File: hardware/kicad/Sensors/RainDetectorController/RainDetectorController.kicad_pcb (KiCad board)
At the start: 2 copper layers, 54.1 x 44.1 mm, 15 parts, among them J1 Conn_01x04_Socket, J2 Conn_01x04_Socket, J3 HEATER_CTRL, J4 RAIN_SIGNAL, Q1 AO3400A, U1 ICM7555xB

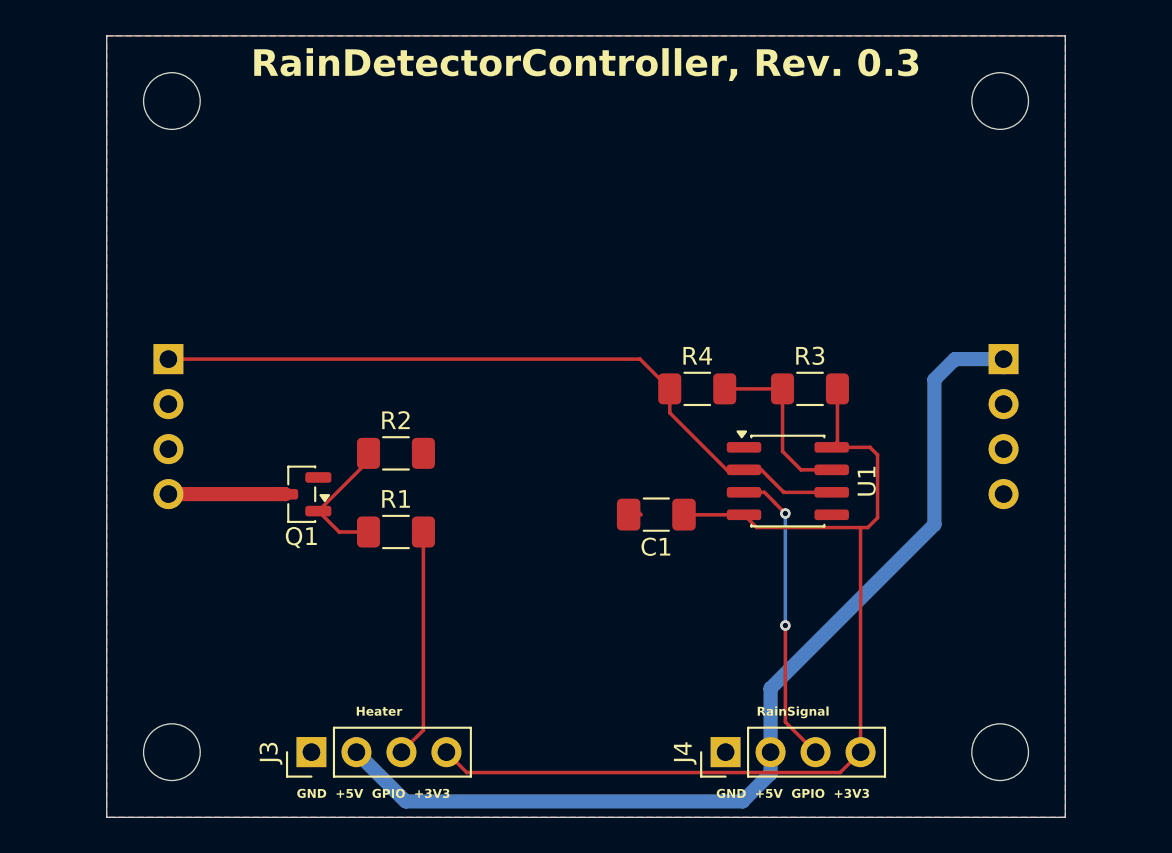
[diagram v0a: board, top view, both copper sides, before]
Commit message: modified Board-Geometry for RainDetector Head & Controller
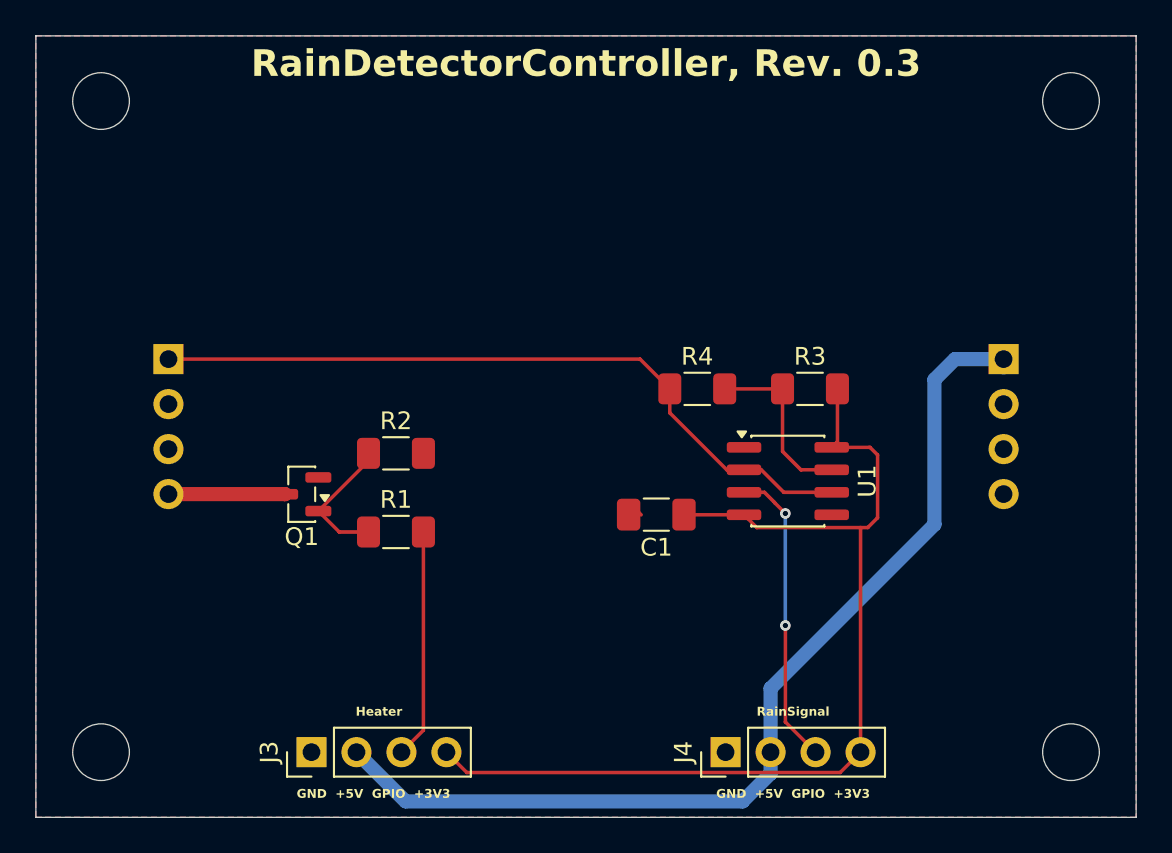
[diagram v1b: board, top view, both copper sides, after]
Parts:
- moved H1 4.00 mm to (71.5, 52.5)
- moved H2 4.00 mm to (126.2, 52.5)
- moved H3 4.00 mm to (126.2, 89.2)
- moved H4 4.00 mm to (71.5, 89.2)
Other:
- board size 54.1 x 44.1 mm -> 62.1 x 44.1 mm
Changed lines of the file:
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@@
 	)
 	(footprint "MountingHole:MountingHole_3.2mm_M3"
-		(locked yes)
 		(layer "F.Cu")
-		(at 75.49 52.45)
+		(at 71.49 52.45)
 		(descr "Mounting Hole 3.2mm, M3, no annular, generated by kicad-footprint-generator mountinghole.py")
 		(tags "mountinghole M3")
@@
 		(locked yes)
 		(layer "F.Cu")
-		(at 122.25 52.45)
+		(at 126.25 52.45)
 		(descr "Mounting Hole 3.2mm, M3, no annular, generated by kicad-footprint-generator mountinghole.py")
 		(tags "mountinghole M3")
@@
 	)
 	(footprint "MountingHole:MountingHole_3.2mm_M3"
-		(locked yes)
 		(layer "F.Cu")
-		(at 122.25 89.21)
+		(at 126.25 89.21)
 		(descr "Mounting Hole 3.2mm, M3, no annular, generated by kicad-footprint-generator mountinghole.py")
 		(tags "mountinghole M3")
@@
 	)
 	(footprint "MountingHole:MountingHole_3.2mm_M3"
-		(locked yes)
 		(layer "F.Cu")
-		(at 75.49 89.21)
+		(at 71.49 89.21)
 		(descr "Mounting Hole 3.2mm, M3, no annular, generated by kicad-footprint-generator mountinghole.py")
 		(tags "mountinghole M3")
@@
 	)
 	(gr_line
-		(start 71.81 45.365)
-		(end 71.81 96.295)
+		(start 67.81 45.365)
+		(end 67.81 96.295)
 		(stroke
 			(width 0.1)
 			(type solid)
 		)
-		(locked yes)
 		(layer "Dwgs.User")
 	)
 	(gr_line
-		(start 71.81 48.77)
-		(end 75.486955 52.446955)
+		(start 67.81 48.77)
+		(end 71.486955 52.446955)
 		(stroke
 			(width 0.1)
@@
 	)
 	(gr_line
-		(start 71.81 92.89)
-		(end 75.486955 89.213045)
+		(start 67.81 92.89)
+		(end 71.486955 89.213045)
 		(stroke
 			(width 0.1)
 			(type solid)
 		)
-		(locked yes)
 		(layer "Dwgs.User")
 	)
@@
 	)
 	(gr_line
-		(start 125.93 48.77)
-		(end 122.253045 52.446955)
+		(start 129.93 48.77)
+		(end 126.253045 52.446955)
 		(stroke
 			(width 0.1)
 			(type solid)
 		)
-		(locked yes)
 		(layer "Dwgs.User")
 	)
 	(gr_rect
-		(start 71.81 48.77)
-		(end 125.93 92.89)
+		(start 67.81 48.77)
+		(end 129.93 92.89)
 		(stroke
 			(width 0.05)
@@
 		)
 		(fill no)
-		(locked yes)
 		(layer "Edge.Cuts")
 	)
@@
 		(polygon
 			(pts
-				(xy 71.81 48.77) (xy 125.93 48.77) (xy 125.93 92.89) (xy 71.81 92.89)
+				(xy 67.8 48.77) (xy 129.93 48.77) (xy 129.93 92.89) (xy 67.8 92.89)
 			)
 		)

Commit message: Update RainDetector board connectors, outlines and parts kits
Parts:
- J1, J2: value Conn_01x04_Socket -> Conn_02x02_Odd_Even; footprint Connector_PinSocket_2.54mm:PinSocket_1x04_P2.54mm_Vertical -> Connector_PinSocket_2.54mm:PinSocket_2x02_P2.54mm_Vertical
- moved J1 2.84 mm to (123.7, 69.6), turned to 90 degrees
- moved J2 2.84 mm to (76.6, 69.6), turned to 90 degrees
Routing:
- net +5V: track 56.1 -> 64.1 mm
- net HEATER-: track 6.59 -> 10.0 mm
- net SENSE: track 41.4 -> 39.9 mm
